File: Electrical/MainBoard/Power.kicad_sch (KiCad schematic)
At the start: 17 parts, among them J2 3.3V Supply, J3 5V Supply, J4 USB_B_Micro, J5 Battery1, J6 Battery1, SW2 5V Bypass, SW3 All Power Switch, U2 AP2114HA-3.3TRG1, U3 AP2114HA-3.3TRG1

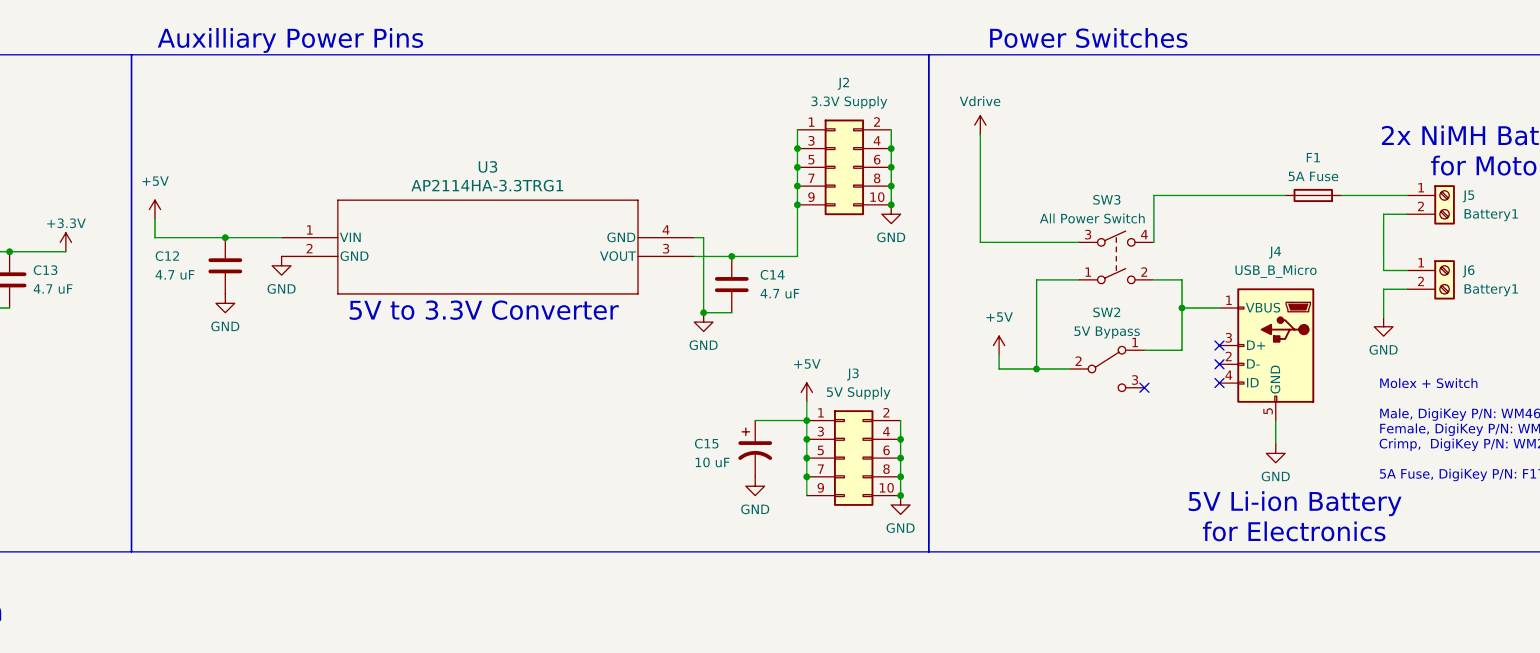
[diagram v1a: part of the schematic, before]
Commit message: Use more molex picoblades and make schematic prettier
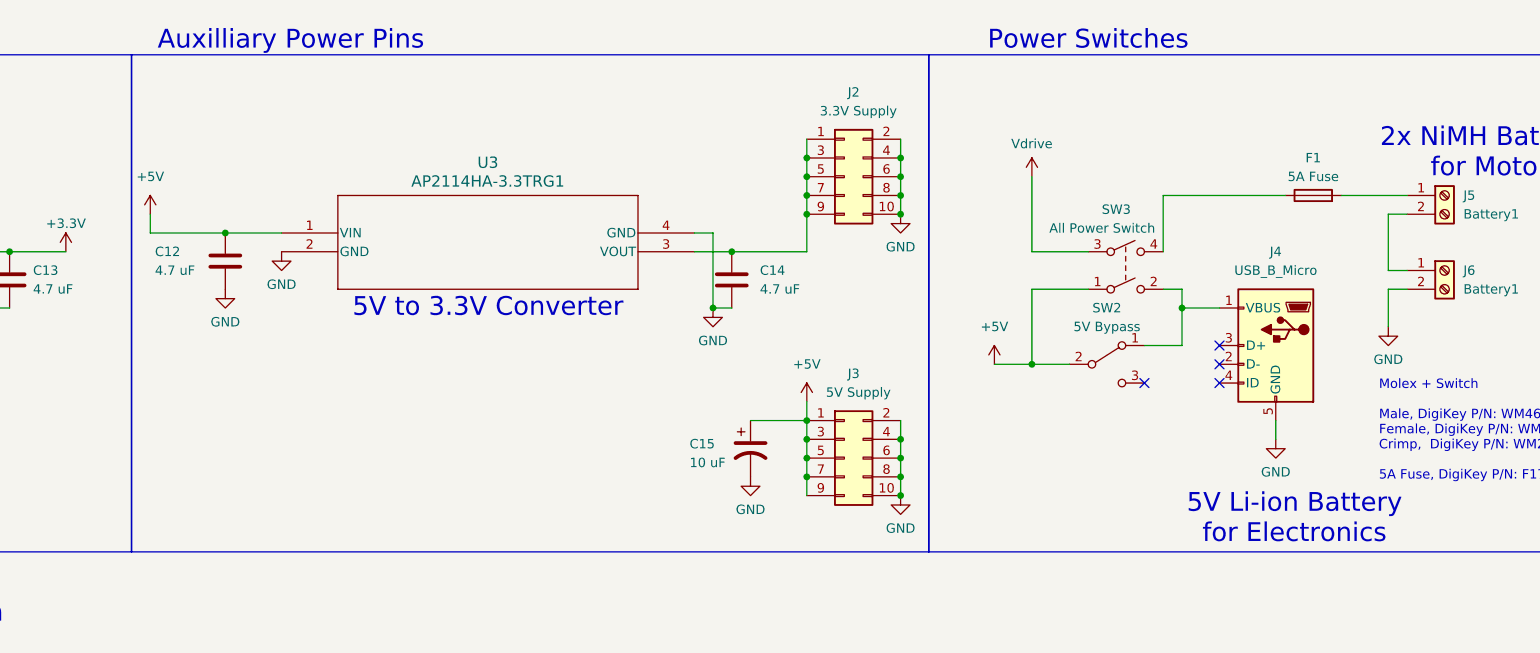
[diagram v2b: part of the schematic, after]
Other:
- moved on the sheet: C12, C14, C15, J2, SW2, SW3, U3
